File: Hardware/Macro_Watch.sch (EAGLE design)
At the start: 28 parts, among them J1 N/P, M1 MF-LED-0805-RED, M16 MF-LED-0805-RED, M2 MF-LED-0805-RED, M32 MF-LED-0805-RED, M4 MF-LED-0805-RED, M8 MF-LED-0805-RED, SW1 MF-SW-TACT-4.2MM, U1 PIC16F527-I/ML, X1 ABS25-32.768KHZ-T

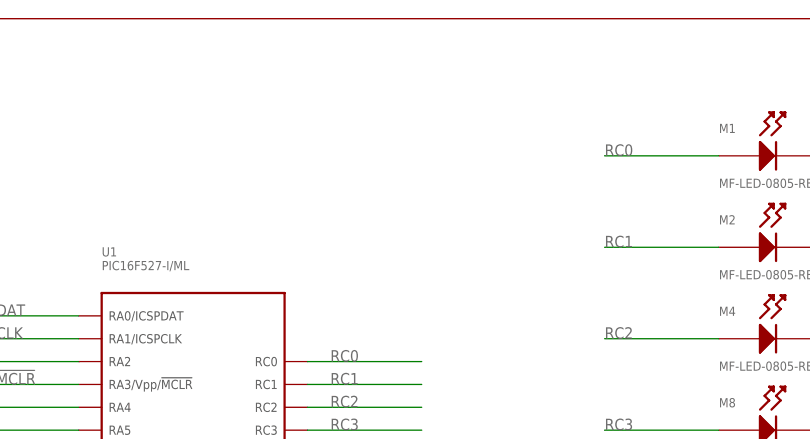
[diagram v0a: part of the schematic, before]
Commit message: Added working camfiles and tweaked layout.
Added a TP for RA2 pin on MCU. Gerber files have been checked and are
ready for production.
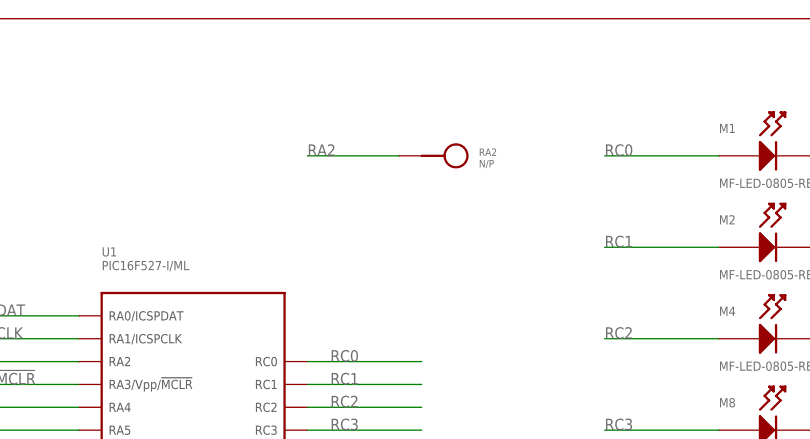
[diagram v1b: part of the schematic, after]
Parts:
- added RA2: N/P, PP_Connectors:TEST_POINT_SINGLEROUND_1MM
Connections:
- net RA2: now also RA2.P$1
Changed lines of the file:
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@@
 <grid distance="0.1" unitdist="inch" unit="inch" style="lines" multiple="1" display="no" altdistance="0.01" altunitdist="inch" altunit="inch"/>
 <layers>
-<layer number="1" name="Top" color="4" fill="1" visible="yes" active="no"/>
-<layer number="2" name="Route2" color="1" fill="3" visible="yes" active="no"/>
-<layer number="3" name="Route3" color="4" fill="3" visible="yes" active="no"/>
-<layer number="4" name="Route4" color="1" fill="4" visible="yes" active="no"/>
-<layer number="5" name="Route5" color="4" fill="4" visible="yes" active="no"/>
-<layer number="6" name="Route6" color="1" fill="8" visible="yes" active="no"/>
-<layer number="7" name="Route7" color="4" fill="8" visible="yes" active="no"/>
-<layer number="8" name="Route8" color="1" fill="2" visible="yes" active="no"/>
-<layer number="9" name="Route9" color="4" fill="2" visible="yes" active="no"/>
-<layer number="10" name="Route10" color="1" fill="7" visible="yes" active="no"/>
-<layer number="11" name="Route11" color="4" fill="7" visible="yes" active="no"/>
-<layer number="12" name="Route12" color="1" fill="5" visible="yes" active="no"/>
-<layer number="13" name="Route13" color="4" fill="5" visible="yes" active="no"/>
-<layer number="14" name="Route14" color="1" fill="6" visible="yes" active="no"/>
-<layer number="15" name="Route15" color="4" fill="6" visible="yes" active="no"/>
-<layer number="16" name="Bottom" color="1" fill="1" visible="yes" active="no"/>
-<layer number="17" name="Pads" color="2" fill="1" visible="yes" active="no"/>
-<layer number="18" name="Vias" color="2" fill="1" visible="yes" active="no"/>
-<layer number="19" name="Unrouted" color="6" fill="1" visible="yes" active="no"/>
-<layer number="20" name="Dimension" color="15" fill="1" visible="yes" active="no"/>
-<layer number="21" name="tPlace" color="7" fill="1" visible="yes" active="no"/>
-<layer number="22" name="bPlace" color="7" fill="1" visible="yes" active="no"/>
-<layer number="23" name="tOrigins" color="15" fill="1" visible="yes" active="no"/>
-<layer number="24" name="bOrigins" color="15" fill="1" visible="yes" active="no"/>
-<layer number="25" name="tNames" color="7" fill="1" visible="yes" active="no"/>
-<layer number="26" name="bNames" color="7" fill="1" visible="yes" active="no"/>
-<layer number="27" name="tValues" color="7" fill="1" visible="yes" active="no"/>
-<layer number="28" name="bValues" color="7" fill="1" visible="yes" active="no"/>
+<layer number="1" name="Top" color="4" fill="1" visible="no" active="no"/>
+<layer number="2" name="Route2" color="1" fill="3" visible="no" active="no"/>
+<layer number="3" name="Route3" color="4" fill="3" visible="no" active="no"/>
+<layer number="4" name="Route4" color="1" fill="4" visible="no" active="no"/>
+<layer number="5" name="Route5" color="4" fill="4" visible="no" active="no"/>
+<layer number="6" name="Route6" color="1" fill="8" visible="no" active="no"/>
+<layer number="7" name="Route7" color="4" fill="8" visible="no" active="no"/>
+<layer number="8" name="Route8" color="1" fill="2" visible="no" active="no"/>
+<layer number="9" name="Route9" color="4" fill="2" visible="no" active="no"/>
+<layer number="10" name="Route10" color="1" fill="7" visible="no" active="no"/>
+<layer number="11" name="Route11" color="4" fill="7" visible="no" active="no"/>
+<layer number="12" name="Route12" color="1" fill="5" visible="no" active="no"/>
+<layer number="13" name="Route13" color="4" fill="5" visible="no" active="no"/>
+<layer number="14" name="Route14" color="1" fill="6" visible="no" active="no"/>
+<layer number="15" name="Route15" color="4" fill="6" visible="no" active="no"/>
+<layer number="16" name="Bottom" color="1" fill="1" visible="no" active="no"/>
+<layer number="17" name="Pads" color="2" fill="1" visible="no" active="no"/>
+<layer number="18" name="Vias" color="2" fill="1" visible="no" active="no"/>
+<layer number="19" name="Unrouted" color="6" fill="1" visible="no" active="no"/>
+<layer number="20" name="Dimension" color="15" fill="1" visible="no" active="no"/>
+<layer number="21" name="tPlace" color="7" fill="1" visible="no" active="no"/>
+<layer number="22" name="bPlace" color="7" fill="1" visible="no" active="no"/>
+<layer number="23" name="tOrigins" color="15" fill="1" visible="no" active="no"/>
+<layer number="24" name="bOrigins" color="15" fill="1" visible="no" active="no"/>
+<layer number="25" name="tNames" color="7" fill="1" visible="no" active="no"/>
+<layer number="26" name="bNames" color="7" fill="1" visible="no" active="no"/>
+<layer number="27" name="tValues" color="7" fill="1" visible="no" active="no"/>
+<layer number="28" name="bValues" color="7" fill="1" visible="no" active="no"/>
 <layer number="29" name="tStop" color="7" fill="3" visible="no" active="no"/>
 <layer number="30" name="bStop" color="7" fill="6" visible="no" active="no"/>
@@
 <layer number="35" name="tGlue" color="7" fill="4" visible="no" active="no"/>
 <layer number="36" name="bGlue" color="7" fill="5" visible="no" active="no"/>
-<layer number="37" name="tTest" color="7" fill="1" visible="yes" active="no"/>
-<layer number="38" name="bTest" color="7" fill="1" visible="yes" active="no"/>
+<layer number="37" name="tTest" color="7" fill="1" visible="no" active="no"/>
+<layer number="38" name="bTest" color="7" fill="1" visible="no" active="no"/>
 <layer number="39" name="tKeepout" color="4" fill="11" visible="no" active="no"/>
 <layer number="40" name="bKeepout" color="1" fill="11" visible="no" active="no"/>
@@
 <layer number="44" name="Drills" color="7" fill="1" visible="no" active="no"/>
 <layer number="45" name="Holes" color="7" fill="1" visible="no" active="no"/>
-<layer number="46" name="Milling" color="3" fill="1" visible="yes" active="no"/>
-<layer number="47" name="Measures" color="7" fill="1" visible="yes" active="no"/>
-<layer number="48" name="Document" color="7" fill="1" visible="yes" active="no"/>
-<layer number="49" name="Reference" color="7" fill="1" visible="yes" active="no"/>
-<layer number="50" name="dxf" color="7" fill="1" visible="yes" active="no"/>
-<layer number="51" name="tDocu" color="7" fill="1" visible="yes" active="no"/>
-<layer number="52" name="bDocu" color="7" fill="1" visible="yes" active="no"/>
-<layer number="53" name="tGND_GNDA" color="7" fill="9" visible="yes" active="no"/>
-<layer number="54" name="bGND_GNDA" color="1" fill="9" visible="yes" active="no"/>
-<layer number="56" name="wert" color="7" fill="1" visible="yes" active="no"/>
+<layer number="46" name="Milling" color="3" fill="1" visible="no" active="no"/>
+<layer number="47" name="Measures" color="7" fill="1" visible="no" active="no"/>
+<layer number="48" name="Document" color="7" fill="1" visible="no" active="no"/>
+<layer number="49" name="Reference" color="7" fill="1" visible="no" active="no"/>
+<layer number="50" name="dxf" color="7" fill="1" visible="no" active="no"/>
+<layer number="51" name="tDocu" color="7" fill="1" visible="no" active="no"/>
+<layer number="52" name="bDocu" color="7" fill="1" visible="no" active="no"/>
+<layer number="53" name="tGND_GNDA" color="7" fill="9" visible="no" active="no"/>
+<layer number="54" name="bGND_GNDA" color="1" fill="9" visible="no" active="no"/>
+<layer number="56" name="wert" color="7" fill="1" visible="no" active="no"/>
 <layer number="91" name="Nets" color="2" fill="1" visible="yes" active="yes"/>
 <layer number="92" name="Busses" color="1" fill="1" visible="yes" active="yes"/>
@@
 <part name="FID4" library="MF_Aesthetics" deviceset="FIDUCIAL" device="_0.5MM"/>
 <part name="U$1" library="PP_Aesthetics" deviceset="MF_LOGO" device="LOGO_SMALL"/>
+<part name="RA2" library="PP_Connectors" deviceset="TEST_POINT_SINGLE" device="ROUND_1MM" value="N/P"/>
 </parts>
 <sheets>
@@
 <instance part="FID4" gate="G$1" x="-22.86" y="33.02"/>
 <instance part="U$1" gate="G$1" x="-10.16" y="22.86"/>
+<instance part="RA2" gate="G$1" x="-104.14" y="147.32"/>
 </instances>
 <busses>
@@
 <label x="-154.94" y="124.46" size="1.27" layer="95" font="vector"/>
 </segment>
-</net>
+<segment>
+<wire x1="-106.68" y1="147.32" x2="-116.84" y2="147.32" width="0.1524" layer="91"/>
+<label x="-116.84" y="147.32" size="1.27" layer="95" font="vector"/>
+<pinref part="RA2" gate="G$1" pin="P$1"/>
+</segment>
+</net>

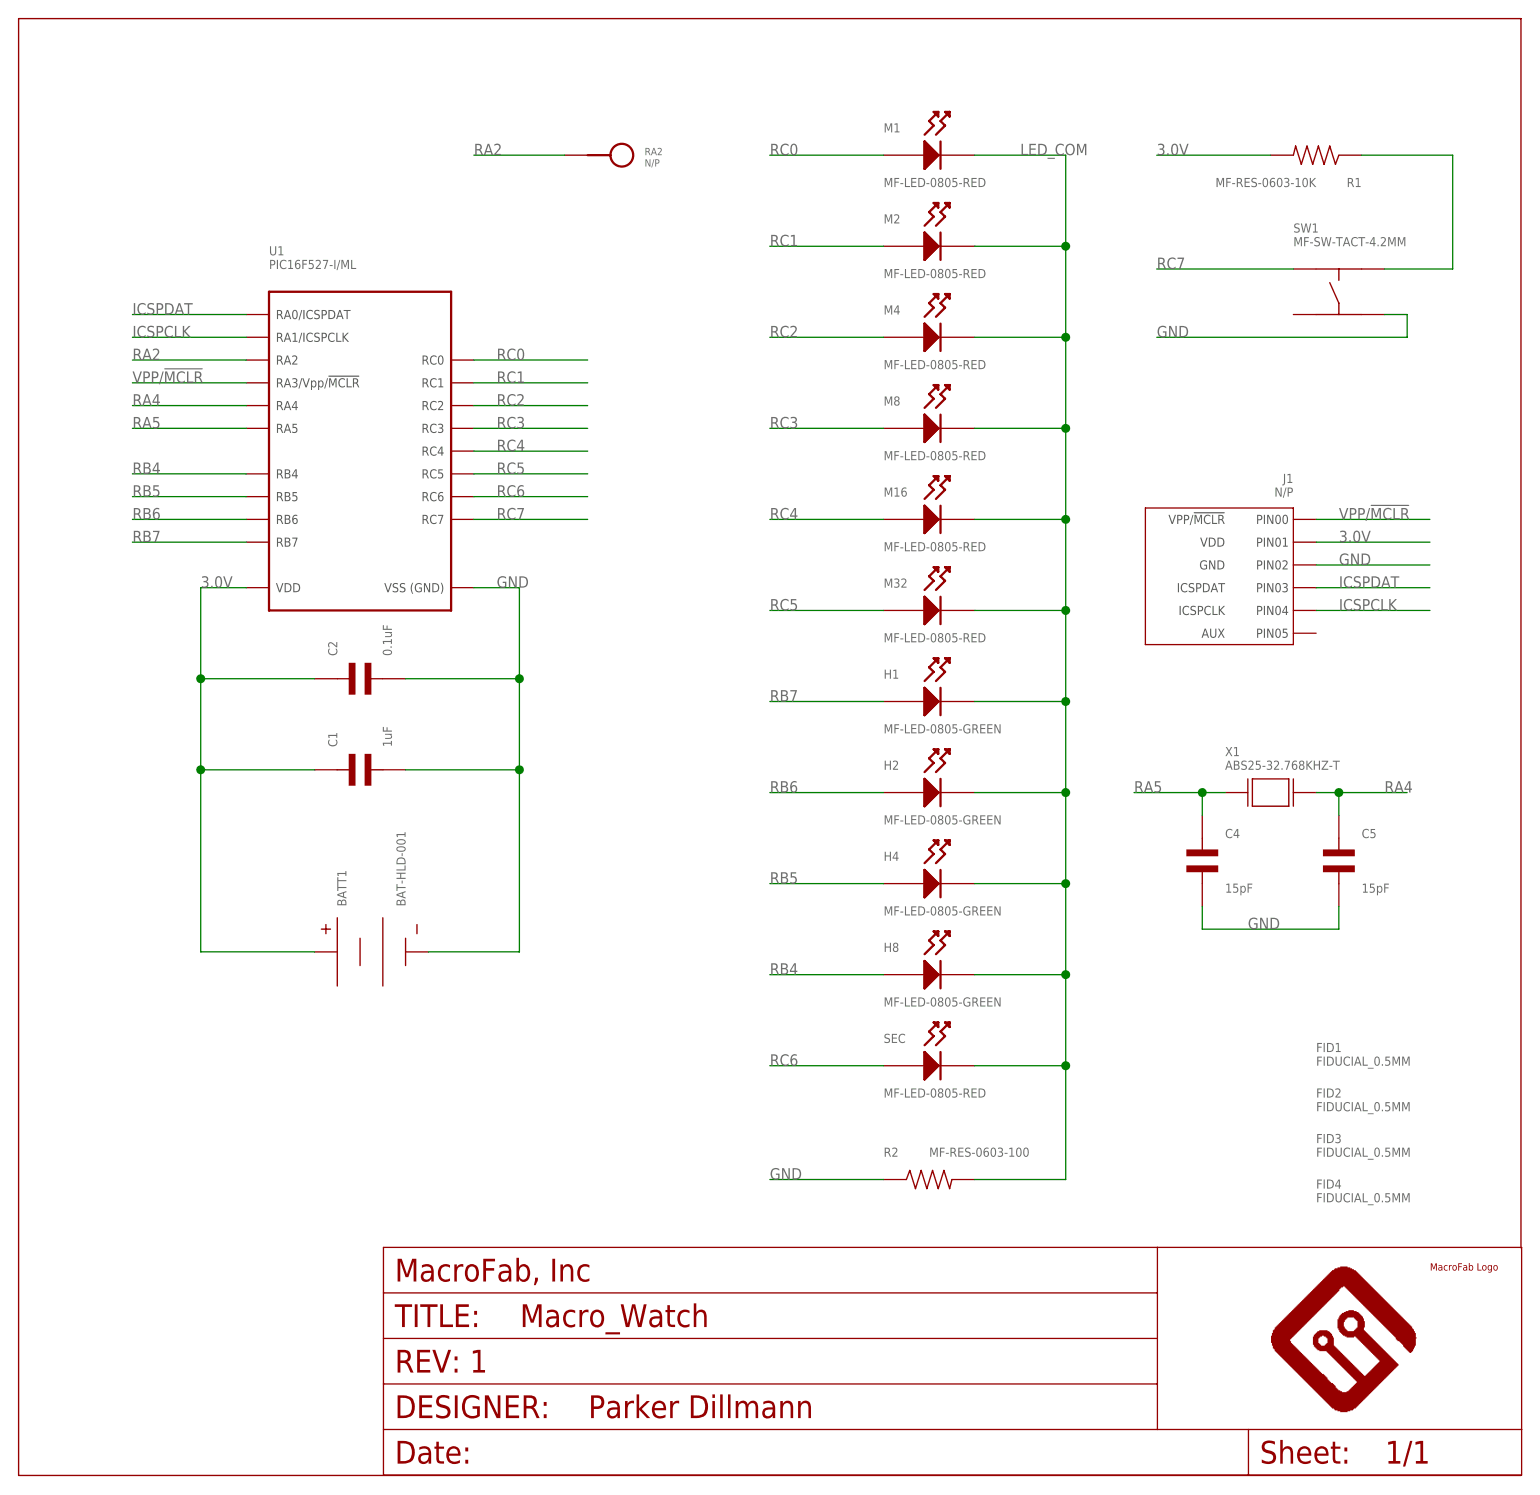
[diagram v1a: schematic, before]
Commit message: Updated TP to latest Library Style.
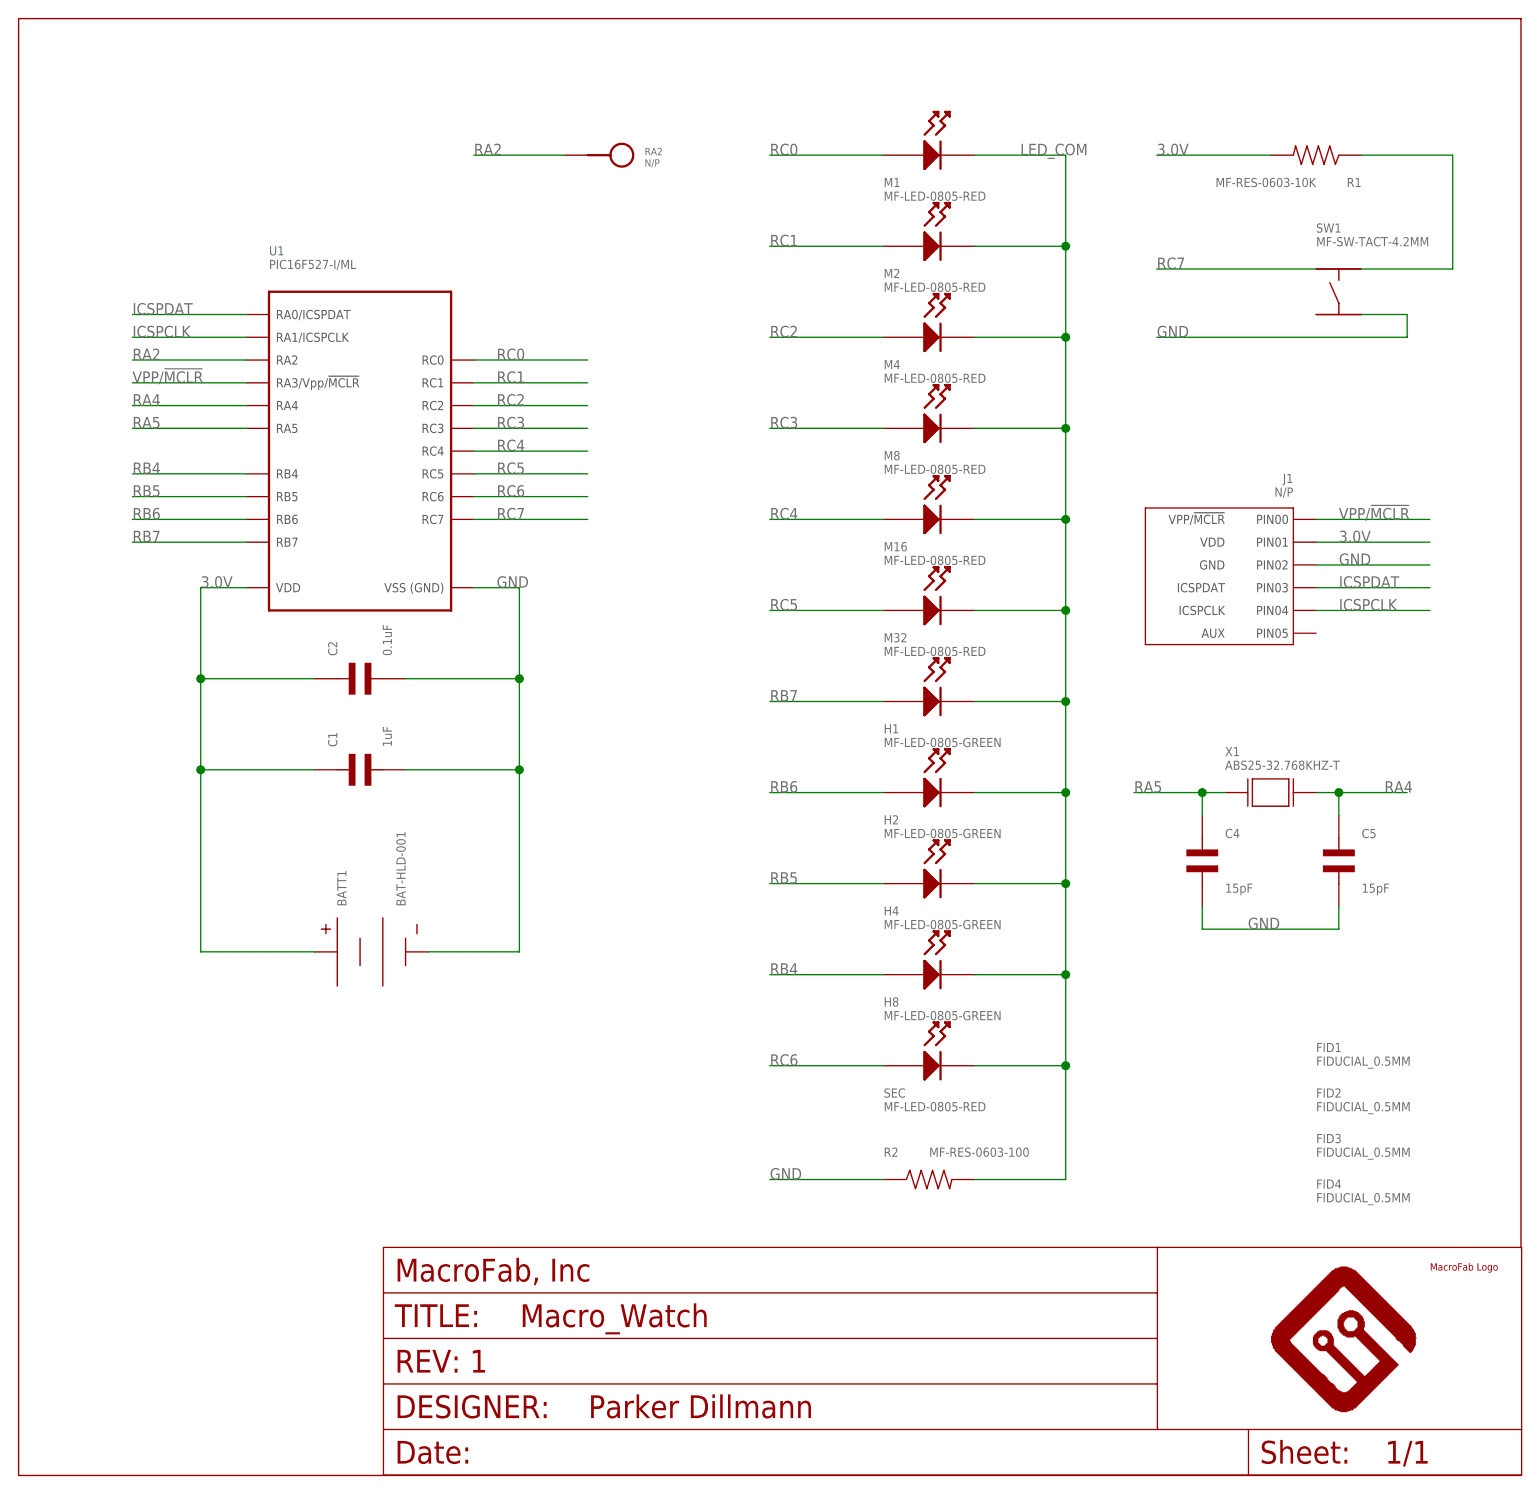
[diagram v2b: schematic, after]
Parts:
- RA2: device PP_Connectors:TEST_POINT_SINGLEROUND_1MM -> PP_Connectors:TEST_POINT_SINGLE_ROUND_1MM
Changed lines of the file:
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@@
 <?xml version="1.0" encoding="utf-8"?>
 <!DOCTYPE eagle SYSTEM "eagle.dtd">
-<eagle version="6.5.0">
+<eagle version="6.6.0">
 <drawing>
 <settings>
@@
 <part name="FID4" library="MF_Aesthetics" deviceset="FIDUCIAL" device="_0.5MM"/>
 <part name="U$1" library="PP_Aesthetics" deviceset="MF_LOGO" device="LOGO_SMALL"/>
-<part name="RA2" library="PP_Connectors" deviceset="TEST_POINT_SINGLE" device="ROUND_1MM" value="N/P"/>
+<part name="RA2" library="PP_Connectors" deviceset="TEST_POINT_SINGLE" device="_ROUND_1MM" value="N/P"/>
 </parts>
 <sheets>
@@
 <segment>
 <pinref part="SW1" gate="G$1" pin="P$4"/>
-<wire x1="-12.7" y1="129.54" x2="-15.24" y2="129.54" width="0.1524" layer="91"/>
+<wire x1="-12.7" y1="129.54" x2="-17.78" y2="129.54" width="0.1524" layer="91"/>
 <wire x1="-12.7" y1="127" x2="-12.7" y2="129.54" width="0.1524" layer="91"/>
 <wire x1="-40.64" y1="127" x2="-12.7" y2="127" width="0.1524" layer="91"/>
@@
 <segment>
 <pinref part="SW1" gate="G$1" pin="P$1"/>
-<wire x1="-25.4" y1="134.62" x2="-40.64" y2="134.62" width="0.1524" layer="91"/>
+<wire x1="-22.86" y1="134.62" x2="-40.64" y2="134.62" width="0.1524" layer="91"/>
 <label x="-40.64" y="134.62" size="1.27" layer="95" font="vector"/>
 </segment>
@@
 <pinref part="SW1" gate="G$1" pin="P$2"/>
 <pinref part="R1" gate="G$1" pin="P$1"/>
-<wire x1="-15.24" y1="134.62" x2="-7.62" y2="134.62" width="0.1524" layer="91"/>
+<wire x1="-17.78" y1="134.62" x2="-7.62" y2="134.62" width="0.1524" layer="91"/>
 <wire x1="-7.62" y1="134.62" x2="-7.62" y2="147.32" width="0.1524" layer="91"/>
 <wire x1="-7.62" y1="147.32" x2="-17.78" y2="147.32" width="0.1524" layer="91"/>
